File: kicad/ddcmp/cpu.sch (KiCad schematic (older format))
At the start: 9 parts, among them J1 UART, J4 LOOPTEST, U1 Pico

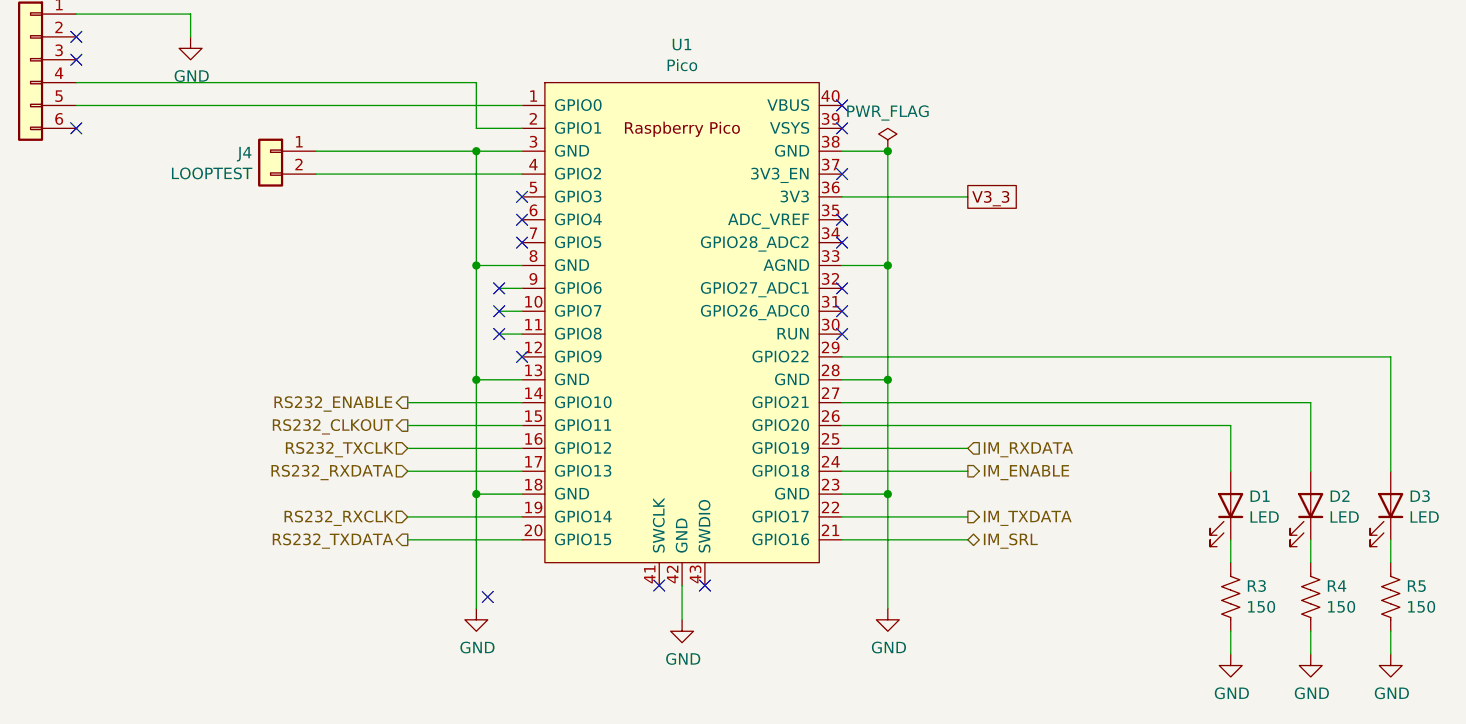
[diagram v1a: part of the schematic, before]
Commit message: Complete schematic, PCB layout, and matching code.  Needs testing.
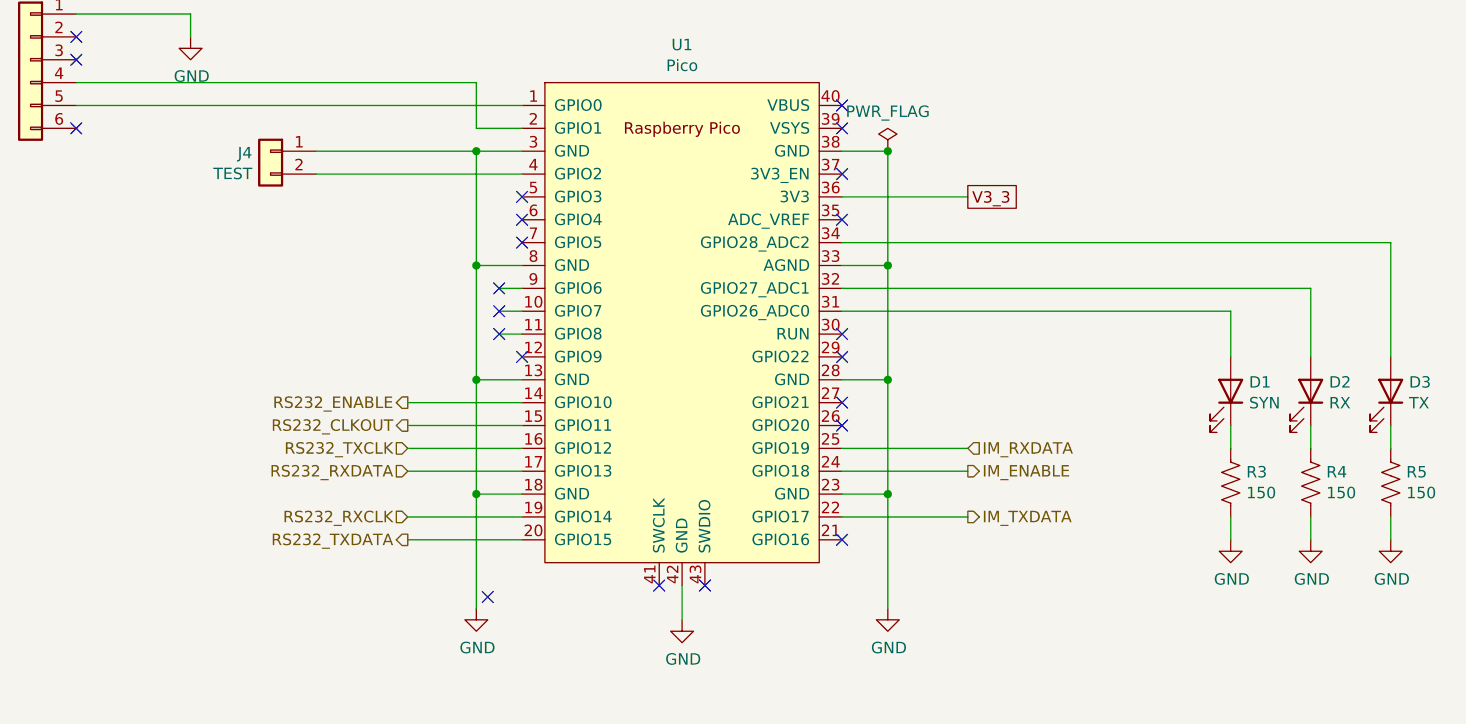
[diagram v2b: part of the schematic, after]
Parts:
- D1: value LED -> SYN; footprint LEDs:LED_D3.0mm -> ddcmp_parts:LED_D3.0mm
- D2: value LED -> RX; footprint LEDs:LED_D3.0mm -> ddcmp_parts:LED_D3.0mm
- D3: value LED -> TX; footprint LEDs:LED_D3.0mm -> ddcmp_parts:LED_D3.0mm
- J4: value LOOPTEST -> TEST; footprint Pin_Headers:Pin_Header_Straight_1x02_Pitch2.54mm -> ddcmp_parts:Pin_Header_Straight_1x02_Pitch2.54mm
- R3, R4, R5: footprint ddcmp_parts:R_Axial_DIN0207_L6.3mm_D2.5mm_P7.62mm_Horizontal -> ddcmp_parts:R_Axial_DIN0207_L6.3mm_D2.5mm_P10.16mm_Horizontal
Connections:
- net at U1.26 (GPIO20): no longer D1.2 (A)
- net at U1.27 (GPIO21): no longer D2.2 (A)
- net at U1.29 (GPIO22): no longer D3.2 (A)
- net at U1.31 (GPIO26_ADC0): now also D1.2 (A)
- net at U1.32 (GPIO27_ADC1): now also D2.2 (A)
- net at U1.34 (GPIO28_ADC2): now also D3.2 (A)
- net IM_SRL: no longer names the net of U1.21 (GPIO16)
- no-connect marks 21 -> 22
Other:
- moved on the sheet: D1, D2, D3, R3, R4, R5
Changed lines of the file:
@@
 $Descr A4 11693 8268
 encoding utf-8
-Sheet 2 4
+Sheet 4 4
 Title "DDCMP Framer"
 Date "2021-05-17"
 Rev "A"
 Comp "AK Design"
-Comment1 ""
+Comment1 "Copyright © 2021 by Paul Koning, NI1D"
 Comment2 ""
 Comment3 ""
@@
 L Device:LED D1
 U 1 1 60AC703D
-P 8350 4300
-F 0 "D1" V 8389 4380 50  0000 L CNN
-F 1 "LED" V 8298 4380 50  0000 L CNN
-F 2 "LEDs:LED_D3.0mm" H 8350 4300 50  0001 C CNN
-F 3 "~" H 8350 4300 50  0001 C CNN
-	1    8350 4300
+P 8350 3800
+F 0 "D1" V 8389 3880 50  0000 L CNN
+F 1 "SYN" V 8298 3880 50  0000 L CNN
+F 2 "ddcmp_parts:LED_D3.0mm" H 8350 3800 50  0001 C CNN
+F 3 "~" H 8350 3800 50  0001 C CNN
+	1    8350 3800
 	0    1    -1   0
 $EndComp
@@
 L Device:LED D2
 U 1 1 60AC83AC
-P 8700 4300
-F 0 "D2" V 8739 4380 50  0000 L CNN
-F 1 "LED" V 8648 4380 50  0000 L CNN
-F 2 "LEDs:LED_D3.0mm" H 8700 4300 50  0001 C CNN
-F 3 "~" H 8700 4300 50  0001 C CNN
-	1    8700 4300
+P 8700 3800
+F 0 "D2" V 8739 3880 50  0000 L CNN
+F 1 "RX" V 8648 3880 50  0000 L CNN
+F 2 "ddcmp_parts:LED_D3.0mm" H 8700 3800 50  0001 C CNN
+F 3 "~" H 8700 3800 50  0001 C CNN
+	1    8700 3800
 	0    1    -1   0
 $EndComp
@@
 L Device:LED D3
 U 1 1 60AC89D4
-P 9050 4300
-F 0 "D3" V 9089 4380 50  0000 L CNN
-F 1 "LED" V 8998 4380 50  0000 L CNN
-F 2 "LEDs:LED_D3.0mm" H 9050 4300 50  0001 C CNN
-F 3 "~" H 9050 4300 50  0001 C CNN
-	1    9050 4300
+P 9050 3800
+F 0 "D3" V 9089 3880 50  0000 L CNN
+F 1 "TX" V 8998 3880 50  0000 L CNN
+F 2 "ddcmp_parts:LED_D3.0mm" H 9050 3800 50  0001 C CNN
+F 3 "~" H 9050 3800 50  0001 C CNN
+	1    9050 3800
 	0    1    -1   0
 $EndComp
@@
 L ddcmp_symbols:R_US R3
 U 1 1 60ACA428
-P 8350 4700
-F 0 "R3" H 8418 4746 50  0000 L CNN
-F 1 "150" H 8418 4655 50  0000 L CNN
-F 2 "ddcmp_parts:R_Axial_DIN0207_L6.3mm_D2.5mm_P7.62mm_Horizontal" V 8390 4690 50  0001 C CNN
-F 3 "" H 8350 4700 50  0001 C CNN
-	1    8350 4700
+P 8350 4200
+F 0 "R3" H 8418 4246 50  0000 L CNN
+F 1 "150" H 8418 4155 50  0000 L CNN
+F 2 "ddcmp_parts:R_Axial_DIN0207_L6.3mm_D2.5mm_P10.16mm_Horizontal" V 8390 4190 50  0001 C CNN
+F 3 "" H 8350 4200 50  0001 C CNN
+	1    8350 4200
 	1    0    0    -1
 $EndComp
@@
 L ddcmp_symbols:R_US R4
 U 1 1 60ACAA45
-P 8700 4700
-F 0 "R4" H 8768 4746 50  0000 L CNN
-F 1 "150" H 8768 4655 50  0000 L CNN
-F 2 "ddcmp_parts:R_Axial_DIN0207_L6.3mm_D2.5mm_P7.62mm_Horizontal" V 8740 4690 50  0001 C CNN
-F 3 "" H 8700 4700 50  0001 C CNN
-	1    8700 4700
+P 8700 4200
+F 0 "R4" H 8768 4246 50  0000 L CNN
+F 1 "150" H 8768 4155 50  0000 L CNN
+F 2 "ddcmp_parts:R_Axial_DIN0207_L6.3mm_D2.5mm_P10.16mm_Horizontal" V 8740 4190 50  0001 C CNN
+F 3 "" H 8700 4200 50  0001 C CNN
+	1    8700 4200
 	1    0    0    -1
 $EndComp
@@
 L ddcmp_symbols:R_US R5
 U 1 1 60ACB075
-P 9050 4700
-F 0 "R5" H 9118 4746 50  0000 L CNN
-F 1 "150" H 9118 4655 50  0000 L CNN
-F 2 "ddcmp_parts:R_Axial_DIN0207_L6.3mm_D2.5mm_P7.62mm_Horizontal" V 9090 4690 50  0001 C CNN
-F 3 "" H 9050 4700 50  0001 C CNN
-	1    9050 4700
+P 9050 4200
+F 0 "R5" H 9118 4246 50  0000 L CNN
+F 1 "150" H 9118 4155 50  0000 L CNN
+F 2 "ddcmp_parts:R_Axial_DIN0207_L6.3mm_D2.5mm_P10.16mm_Horizontal" V 9090 4190 50  0001 C CNN
+F 3 "" H 9050 4200 50  0001 C CNN
+	1    9050 4200
 	1    0    0    -1
 $EndComp
@@
 L power:GND #PWR0111
 U 1 1 60ACBBD7
-P 8350 4950
-F 0 "#PWR0111" H 8350 4700 50  0001 C CNN
-F 1 "GND" H 8355 4777 50  0000 C CNN
-F 2 "" H 8350 4950 50  0001 C CNN
-F 3 "" H 8350 4950 50  0001 C CNN
-	1    8350 4950
+P 8350 4450
+F 0 "#PWR0111" H 8350 4200 50  0001 C CNN
+F 1 "GND" H 8355 4277 50  0000 C CNN
+F 2 "" H 8350 4450 50  0001 C CNN
+F 3 "" H 8350 4450 50  0001 C CNN
+	1    8350 4450
 	1    0    0    -1
 $EndComp
@@
 L power:GND #PWR0112
 U 1 1 60ACC03F
-P 8700 4950
-F 0 "#PWR0112" H 8700 4700 50  0001 C CNN
-F 1 "GND" H 8705 4777 50  0000 C CNN
-F 2 "" H 8700 4950 50  0001 C CNN
-F 3 "" H 8700 4950 50  0001 C CNN
-	1    8700 4950
+P 8700 4450
+F 0 "#PWR0112" H 8700 4200 50  0001 C CNN
+F 1 "GND" H 8705 4277 50  0000 C CNN
+F 2 "" H 8700 4450 50  0001 C CNN
+F 3 "" H 8700 4450 50  0001 C CNN
+	1    8700 4450
 	1    0    0    -1
 $EndComp
@@
 L power:GND #PWR0113
 U 1 1 60ACC9AB
-P 9050 4950
-F 0 "#PWR0113" H 9050 4700 50  0001 C CNN
-F 1 "GND" H 9055 4777 50  0000 C CNN
-F 2 "" H 9050 4950 50  0001 C CNN
-F 3 "" H 9050 4950 50  0001 C CNN
-	1    9050 4950
-	1    0    0    -1
-$EndComp
-Wire Wire Line
-	9050 4950 9050 4850
-Wire Wire Line
-	8700 4950 8700 4850
-Wire Wire Line
-	8350 4950 8350 4850
-Wire Wire Line
-	8350 4550 8350 4450
-Wire Wire Line
-	8700 4550 8700 4450
-Wire Wire Line
-	9050 4550 9050 4450
+P 9050 4450
+F 0 "#PWR0113" H 9050 4200 50  0001 C CNN
+F 1 "GND" H 9055 4277 50  0000 C CNN
+F 2 "" H 9050 4450 50  0001 C CNN
+F 3 "" H 9050 4450 50  0001 C CNN
+	1    9050 4450
+	1    0    0    -1
+$EndComp
+Wire Wire Line
+	9050 4450 9050 4350
+Wire Wire Line
+	8700 4450 8700 4350
+Wire Wire Line
+	8350 4450 8350 4350
+Wire Wire Line
+	8350 4050 8350 3950
+Wire Wire Line
+	8700 4050 8700 3950
+Wire Wire Line
+	9050 4050 9050 3950
 Wire Wire Line
 	6650 4350 7200 4350
@@
 Wire Wire Line
 	5250 4450 4750 4450
-Text HLabel 7200 4450 2    50   3State ~ 0
-IM_SRL
 Text HLabel 7200 4150 2    50   Output ~ 0
 IM_ENABLE
@@
 P 4150 2750
 F 0 "J4" H 4230 2742 50  0000 L CNN
-F 1 "LOOPTEST" H 4230 2651 50  0000 L CNN
-F 2 "Pin_Headers:Pin_Header_Straight_1x02_Pitch2.54mm" H 4150 2750 50  0001 C CNN
+F 1 "TEST" H 4230 2651 50  0000 L CNN
+F 2 "ddcmp_parts:Pin_Header_Straight_1x02_Pitch2.54mm" H 4150 2750 50  0001 C CNN
 F 3 "~" H 4150 2750 50  0001 C CNN
 	1    4150 2750
@@
 NoConn ~ 6650 2850
 NoConn ~ 6650 3050
-NoConn ~ 6650 3150
-NoConn ~ 6650 3350
-NoConn ~ 6650 3450
 NoConn ~ 6650 3550
 NoConn ~ 5100 4700
@@
 	6650 2950 7200 2950
 Wire Wire Line
-	6650 4450 7200 4450
-Wire Wire Line
 	7200 4050 6650 4050
 Wire Wire Line
@@
 	4350 2850 5250 2850
 Wire Wire Line
-	6650 3950 8350 3950
-Wire Wire Line
-	8350 3950 8350 4150
-Wire Wire Line
-	8700 4150 8700 3850
-Wire Wire Line
-	8700 3850 6650 3850
-Wire Wire Line
-	6650 3650 9050 3650
-Wire Wire Line
-	9050 3650 9050 4150
+	6650 3450 8350 3450
+Wire Wire Line
+	8350 3450 8350 3650
+Wire Wire Line
+	8700 3650 8700 3350
+Wire Wire Line
+	8700 3350 6650 3350
+Wire Wire Line
+	6650 3150 9050 3150
+Wire Wire Line
+	9050 3150 9050 3650
 Wire Wire Line
 	5250 3550 5150 3550
@@
 NoConn ~ 5250 3050
 NoConn ~ 5250 2950
+NoConn ~ 6650 3650
+NoConn ~ 6650 3850
+NoConn ~ 6650 3950
+NoConn ~ 6650 4450
 $EndSCHEMATC

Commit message: Schematic and PCB modeling tweaks.
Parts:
- D1: Digikey part (none) -> 1497-1490-ND; Vendor (none) -> SunLED; Vendor part (none) -> XLUG34D
- D2: Digikey part (none) -> 1497-1492-ND; Vendor (none) -> SunLED; Vendor part (none) -> XLUY34D
- D3: Digikey part (none) -> 1497-1491-ND; Vendor (none) -> SunLED; Vendor part (none) -> XLUR34D
- J1: Digikey part (none) -> 952-2269-ND; Vendor (none) -> Harwin Inc.; Vendor part (none) -> M20-9990645
- J4: Digikey part (none) -> 952-2261-ND; Vendor (none) -> Harwin Inc.; Vendor part (none) -> M20-9990245
- R3, R4, R5: Digikey part (none) -> 150QBK-ND; Vendor (none) -> Yageo; Vendor part (none) -> CFR-25JB-52-150R
- U1: Digikey part (none) -> 2648-SC0915CT-ND; Vendor (none) -> Raspberry Pi; Vendor part (none) -> SC0915
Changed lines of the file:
@@
 F 1 "UART" H 3018 2676 50  0000 C CNN
 F 2 "ddcmp_parts:Pin_Header_Straight_1x06_Pitch2.54mm" H 3100 2350 50  0001 C CNN
-F 3 "~" H 3100 2350 50  0001 C CNN
+F 3 "https://cdn.harwin.com/pdfs/C001XX_M20_Series_Connectors.pdf" H 3100 2350 50  0001 C CNN
+F 4 "952-2269-ND" H 3100 2350 50  0001 C CNN "Digikey part"
+F 5 "Harwin Inc." H 3100 2350 50  0001 C CNN "Vendor"
+F 6 "M20-9990645" H 3100 2350 50  0001 C CNN "Vendor part"
 	1    3100 2350
 	-1   0    0    -1
@@
 F 1 "SYN" V 8298 3880 50  0000 L CNN
 F 2 "ddcmp_parts:LED_D3.0mm" H 8350 3800 50  0001 C CNN
-F 3 "~" H 8350 3800 50  0001 C CNN
+F 3 "https://www.sunledusa.com/products/spec/XLUG34D.pdf" H 8350 3800 50  0001 C CNN
+F 4 "1497-1490-ND" H 8350 3800 50  0001 C CNN "Digikey part"
+F 5 "SunLED" H 8350 3800 50  0001 C CNN "Vendor"
+F 6 "XLUG34D" H 8350 3800 50  0001 C CNN "Vendor part"
 	1    8350 3800
 	0    1    -1   0
@@
 F 1 "RX" V 8648 3880 50  0000 L CNN
 F 2 "ddcmp_parts:LED_D3.0mm" H 8700 3800 50  0001 C CNN
-F 3 "~" H 8700 3800 50  0001 C CNN
+F 3 "https://www.sunledusa.com/products/spec/XLUY34D.pdf" H 8700 3800 50  0001 C CNN
+F 4 "1497-1492-ND" H 8700 3800 50  0001 C CNN "Digikey part"
+F 5 "SunLED" H 8700 3800 50  0001 C CNN "Vendor"
+F 6 "XLUY34D" H 8700 3800 50  0001 C CNN "Vendor part"
 	1    8700 3800
 	0    1    -1   0
@@
 F 1 "TX" V 8998 3880 50  0000 L CNN
 F 2 "ddcmp_parts:LED_D3.0mm" H 9050 3800 50  0001 C CNN
-F 3 "~" H 9050 3800 50  0001 C CNN
+F 3 "https://www.sunledusa.com/products/spec/XLUR34D.pdf" H 9050 3800 50  0001 C CNN
+F 4 "1497-1491-ND" H 9050 3800 50  0001 C CNN "Digikey part"
+F 5 "SunLED" H 9050 3800 50  0001 C CNN "Vendor"
+F 6 "XLUR34D" H 9050 3800 50  0001 C CNN "Vendor part"
 	1    9050 3800
 	0    1    -1   0
@@
 F 2 "ddcmp_parts:R_Axial_DIN0207_L6.3mm_D2.5mm_P10.16mm_Horizontal" V 8390 4190 50  0001 C CNN
 F 3 "" H 8350 4200 50  0001 C CNN
+F 4 "150QBK-ND" H 8350 4200 50  0001 C CNN "Digikey part"
+F 5 "Yageo" H 8350 4200 50  0001 C CNN "Vendor"
+F 6 "CFR-25JB-52-150R" H 8350 4200 50  0001 C CNN "Vendor part"
 	1    8350 4200
 	1    0    0    -1
@@
 F 2 "ddcmp_parts:R_Axial_DIN0207_L6.3mm_D2.5mm_P10.16mm_Horizontal" V 8740 4190 50  0001 C CNN
 F 3 "" H 8700 4200 50  0001 C CNN
+F 4 "150QBK-ND" H 8700 4200 50  0001 C CNN "Digikey part"
+F 5 "Yageo" H 8700 4200 50  0001 C CNN "Vendor"
+F 6 "CFR-25JB-52-150R" H 8700 4200 50  0001 C CNN "Vendor part"
 	1    8700 4200
 	1    0    0    -1
@@
 F 2 "ddcmp_parts:R_Axial_DIN0207_L6.3mm_D2.5mm_P10.16mm_Horizontal" V 9090 4190 50  0001 C CNN
 F 3 "" H 9050 4200 50  0001 C CNN
+F 4 "150QBK-ND" H 9050 4200 50  0001 C CNN "Digikey part"
+F 5 "Yageo" H 9050 4200 50  0001 C CNN "Vendor"
+F 6 "CFR-25JB-52-150R" H 9050 4200 50  0001 C CNN "Vendor part"
 	1    9050 4200
 	1    0    0    -1
@@
 F 1 "TEST" H 4230 2651 50  0000 L CNN
 F 2 "ddcmp_parts:Pin_Header_Straight_1x02_Pitch2.54mm" H 4150 2750 50  0001 C CNN
-F 3 "~" H 4150 2750 50  0001 C CNN
+F 3 "https://cdn.harwin.com/pdfs/C001XX_M20_Series_Connectors.pdf" H 4150 2750 50  0001 C CNN
+F 4 "952-2261-ND" H 4150 2750 50  0001 C CNN "Digikey part"
+F 5 "Harwin Inc." H 4150 2750 50  0001 C CNN "Vendor"
+F 6 "M20-9990245" H 4150 2750 50  0001 C CNN "Vendor part"
 	1    4150 2750
 	-1   0    0    -1
@@
 F 1 "Pico" H 5950 4624 50  0000 C CNN
 F 2 "ddcmp_parts:RPi_Pico_SMD_TH" V 5950 3500 50  0001 C CNN
-F 3 "" H 5950 3500 50  0001 C CNN
+F 3 "https://datasheets.raspberrypi.org/pico/pico-datasheet.pdf" H 5950 3500 50  0001 C CNN
+F 4 "2648-SC0915CT-ND " H 5950 3500 50  0001 C CNN "Digikey part"
+F 5 "Raspberry Pi" H 5950 3500 50  0001 C CNN "Vendor"
+F 6 "SC0915" H 5950 3500 50  0001 C CNN "Vendor part"
 	1    5950 3500
 	1    0    0    -1

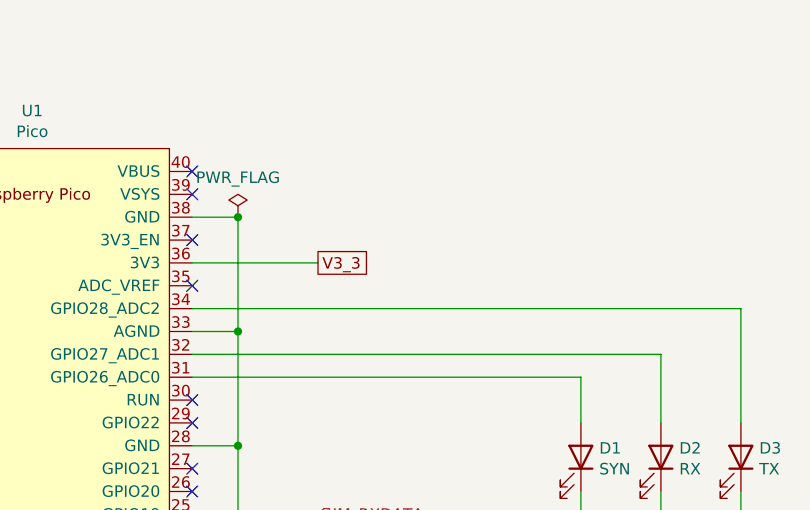
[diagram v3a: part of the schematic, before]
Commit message: Schematics and 3d model cleanups; first drafts of a lot of documentation.
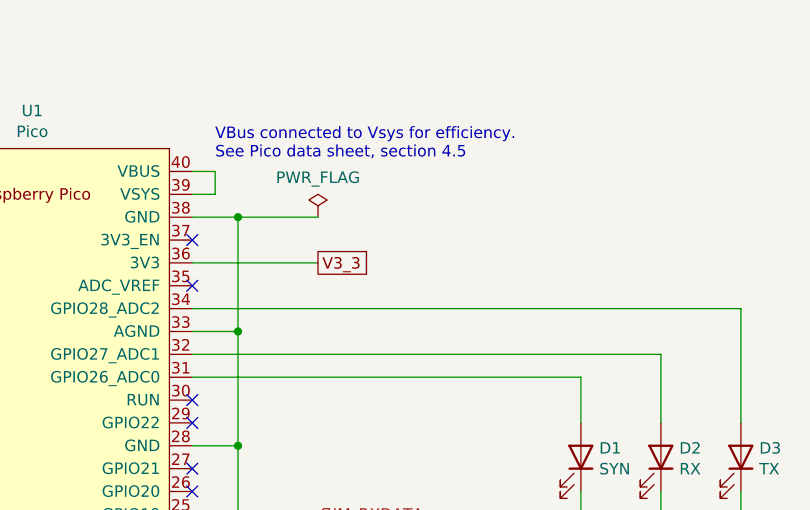
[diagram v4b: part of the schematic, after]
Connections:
- net at U1.39 (VSYS): now also U1.40 (VBUS)
- no-connect marks 22 -> 20
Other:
- note added: "VBus connected to Vsys for efficiency.\nSee Pico data sheet, section 4.5"
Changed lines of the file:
@@
 Wire Wire Line
 	5050 2750 5050 3250
-Wire Wire Line
-	6650 2750 6850 2750
 $Comp
 L power:GND #PWR0101
@@
 $EndComp
 Wire Wire Line
-	6850 2750 6850 3250
-Wire Wire Line
 	6650 3250 6850 3250
-Connection ~ 6850 3250
 Wire Wire Line
 	6850 3250 6850 3750
@@
 NoConn ~ 3300 2650
 NoConn ~ 5250 3150
-NoConn ~ 6650 2550
-NoConn ~ 6650 2650
 NoConn ~ 6650 2850
 NoConn ~ 6650 3050
@@
 NoConn ~ 5850 4650
 NoConn ~ 6050 4650
-$Comp
-L power:PWR_FLAG #FLG0101
-U 1 1 60B1F675
-P 6850 2750
-F 0 "#FLG0101" H 6850 2825 50  0001 C CNN
-F 1 "PWR_FLAG" H 6850 2923 50  0000 C CNN
-F 2 "" H 6850 2750 50  0001 C CNN
-F 3 "~" H 6850 2750 50  0001 C CNN
-	1    6850 2750
-	1    0    0    -1
-$EndComp
-Connection ~ 6850 2750
 $Comp
 L ddcmp_symbols:Raspberry_Pico U?
@@
 NoConn ~ 6650 3950
 NoConn ~ 6650 4450
+Wire Wire Line
+	6650 2750 6850 2750
+$Comp
+L power:PWR_FLAG #FLG0101
+U 1 1 60B1F675
+P 7200 2750
+F 0 "#FLG0101" H 7200 2825 50  0001 C CNN
+F 1 "PWR_FLAG" H 7200 2923 50  0000 C CNN
+F 2 "" H 7200 2750 50  0001 C CNN
+F 3 "~" H 7200 2750 50  0001 C CNN
+	1    7200 2750
+	1    0    0    -1
+$EndComp
+Wire Wire Line
+	6850 3250 6850 2750
+Connection ~ 6850 3250
+Connection ~ 6850 2750
+Wire Wire Line
+	6850 2750 7200 2750
+Wire Wire Line
+	6650 2550 6750 2550
+Wire Wire Line
+	6750 2550 6750 2650
+Wire Wire Line
+	6750 2650 6650 2650
+Text Notes 6750 2500 0    50   ~ 0
+VBus connected to Vsys for efficiency.\nSee Pico data sheet, section 4.5
 $EndSCHEMATC
